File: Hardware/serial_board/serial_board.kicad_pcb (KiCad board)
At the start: 2 copper layers, 80.8 x 60.1 mm, 11 parts, among them J1 Conn_01x40, J2 Conn_01x06, U1 W65C51NxP, X1 CXO_DIP8

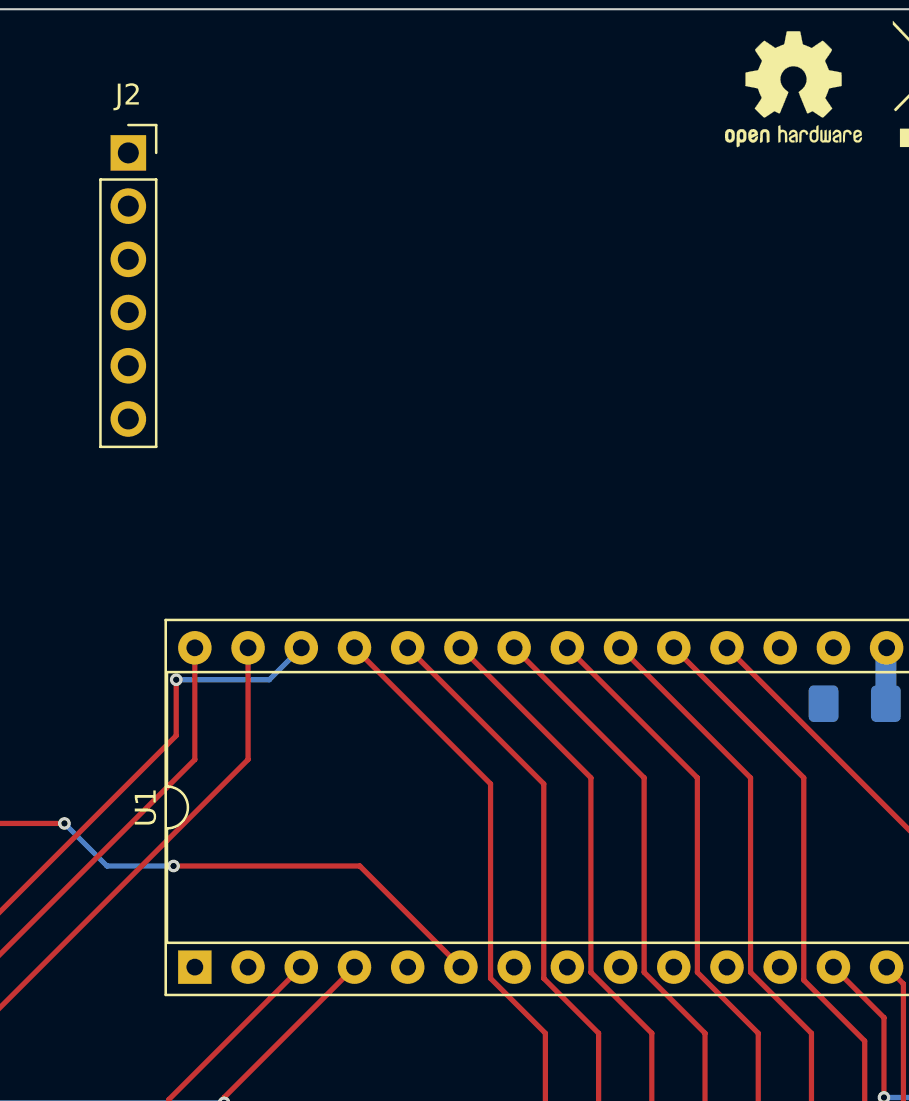
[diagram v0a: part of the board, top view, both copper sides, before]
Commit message: USB serial adapter socket
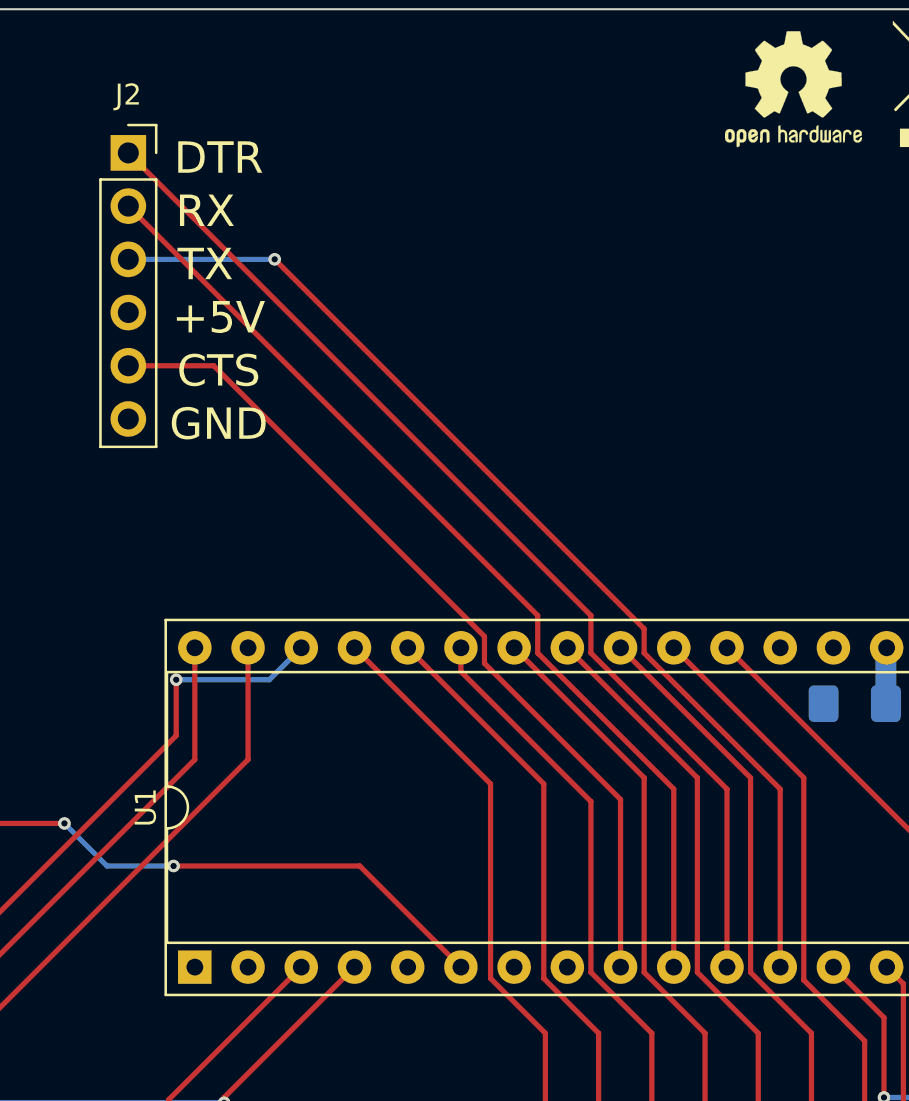
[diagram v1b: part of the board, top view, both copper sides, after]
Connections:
- J2 pad 4: Net-(J2-Pad4) -> +5V
- J2 pad 6: Net-(J2-Pad6) -> GND
- U1 pad 1: Net-(U1-Pad1) -> GND
- U1 pad 10: Net-(U1-Pad10) -> Net-(J2-Pad2)
- U1 pad 11: Net-(U1-Pad11) -> Net-(J2-Pad1)
- U1 pad 12: Net-(U1-Pad12) -> Net-(J2-Pad3)
- U1 pad 16: Net-(U1-Pad16) -> GND
- U1 pad 17: Net-(U1-Pad17) -> GND
- U1 pad 9: Net-(U1-Pad9) -> Net-(J2-Pad5)
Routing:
- net Net-(J2-Pad3): track 0.00 -> 50.8 mm, vias 0 -> 1
- net Net-(J2-Pad1): track 0.00 -> 50.7 mm
- net Net-(J2-Pad2): track 0.00 -> 47.1 mm
- net Net-(J2-Pad5): track 0.00 -> 40.8 mm
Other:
- board text added: "+5V"
- board text added: "CTS"
- board text added: "DTR"
- board text added: "GND"
- board text added: "RX"
- board text added: "TX"
